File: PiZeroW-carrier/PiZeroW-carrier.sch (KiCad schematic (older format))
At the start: 0 parts

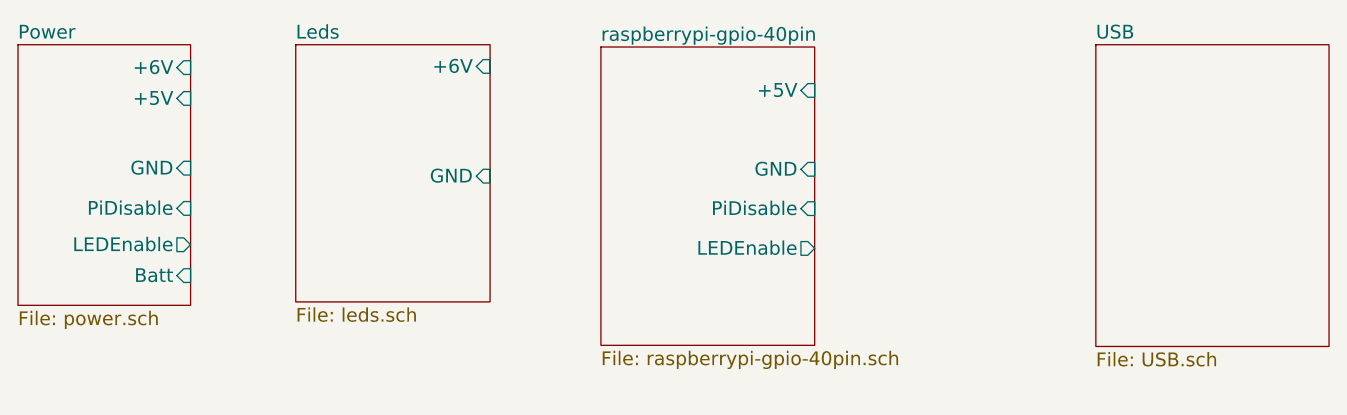
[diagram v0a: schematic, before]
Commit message: fix PiDisable/LEDEnable.  Need to connect them on the root sheet. Extra-duh
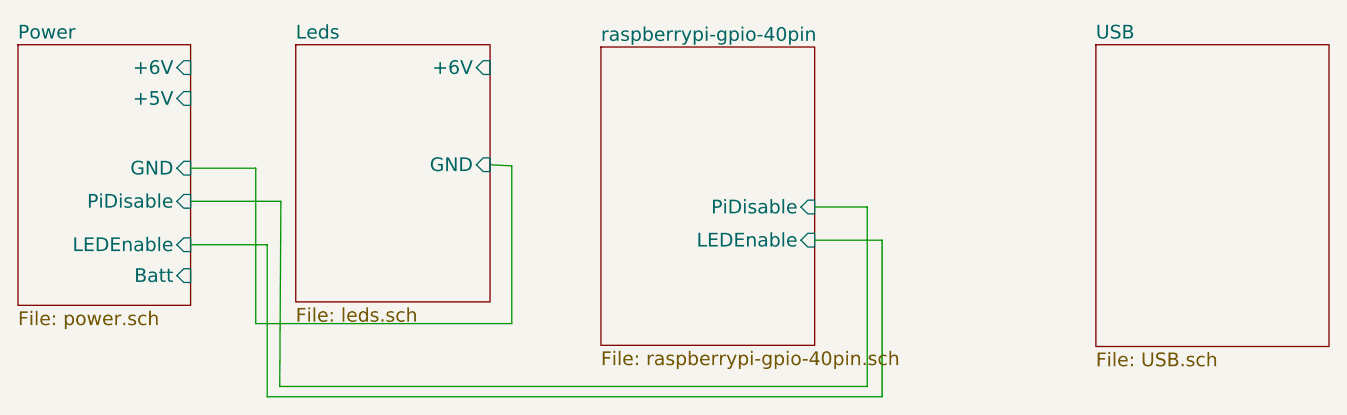
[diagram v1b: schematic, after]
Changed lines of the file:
@@
 F4 "+6V" I R 1900 1300 60
 F5 "+5V" I R 1900 1435 60
-F6 "PiDisable" I R 1900 1916 60
-F7 "LEDEnable" O R 1900 2075 60
+F6 "PiDisable" I R 1900 1885 60
+F7 "LEDEnable" I R 1900 2075 60
 $EndSheet
 $Sheet
@@
 F0 "Leds" 60
 F1 "leds.sch" 60
-F2 "+6V" I R 3210 1295 60
-F3 "GND" I R 3210 1775 60
+F2 "+6V" I R 3210 1300 60
+F3 "GND" I R 3210 1725 60
 $EndSheet
 $Sheet
@@
 F0 "raspberrypi-gpio-40pin" 60
 F1 "raspberrypi-gpio-40pin.sch" 60
-F2 "+5V" I R 4630 1400 60
-F3 "GND" I R 4630 1745 60
-F4 "PiDisable" I R 4630 1917 60
-F5 "LEDEnable" O R 4630 2091 60
+F2 "PiDisable" I R 4630 1910 60
+F3 "LEDEnable" I R 4630 2055 60
 $EndSheet
 $Sheet
@@
 F1 "USB.sch" 60
 $EndSheet
+Wire Wire Line
+	2295 1885 2290 2695
+Wire Wire Line
+	2290 2695 4860 2695
+Wire Wire Line
+	4860 2695 4860 1910
+Wire Wire Line
+	4860 1910 4630 1910
+Wire Wire Line
+	1900 2075 2235 2075
+Wire Wire Line
+	2235 2075 2235 2740
+Wire Wire Line
+	2235 2740 4925 2740
+Wire Wire Line
+	4925 2740 4925 2055
+Wire Wire Line
+	4925 2055 4630 2055
+Wire Wire Line
+	3210 1725 3305 1730
+Wire Wire Line
+	3305 1730 3305 2420
+Wire Wire Line
+	3305 2420 2185 2420
+Wire Wire Line
+	2185 2420 2185 1740
+Wire Wire Line
+	2185 1740 1900 1740
+Wire Wire Line
+	2295 1885 1900 1885
 $EndSCHEMATC
